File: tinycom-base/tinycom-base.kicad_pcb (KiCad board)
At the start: 2 copper layers, 45.2 x 45.2 mm, 48 parts, among them J1 MICRO_SD_HINGE, P1 CONN_02X10, P2 CONN_02X10, P3 USB_A, P4 USB_OTG, U1 SY8008BAAC, U2 AXP209, U3 SY8008BAAC, U4 RTL8188, U5 rainsun-antenna

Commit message: update base
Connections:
- P1 pad 1: (no net) -> HTX2P
- P1 pad 10: UD0_N -> UD1_N
- P1 pad 11: (no net) -> HTX0N
- P1 pad 12: UD1_P -> Net-(P1-Pad12)
- P1 pad 13: (no net) -> HTXCP
- P1 pad 14: UD1_N -> Net-(P1-Pad14)
- P1 pad 15: (no net) -> HTXCN
- P1 pad 16: (no net) -> Net-(P1-Pad16)
- P1 pad 17: (no net) -> HCEC
- P1 pad 18: (no net) -> HHPD
- P1 pad 19: (no net) -> HCSL
- P1 pad 20: (no net) -> HSDA
- P1 pad 3: (no net) -> HTX2N
- P1 pad 4: (no net) -> UD0_P
- P1 pad 5: (no net) -> HTX1P
- P1 pad 6: (no net) -> UD0_N
- P1 pad 7: (no net) -> HTX1N
- P1 pad 8: UD0_P -> UD1_P
- P1 pad 9: (no net) -> HTX0P
- P2 pad 13: (no net) -> Net-(P2-Pad13)
- P2 pad 15: (no net) -> UART1_RX
- P2 pad 17: (no net) -> UART1_TX
- P2 pad 8: (no net) -> Net-(P2-Pad8)
- P4 pad 2: (no net) -> Net-(P4-Pad2)
- P4 pad 3: (no net) -> Net-(P4-Pad3)
- U2 pad 11: (no net) -> Net-(U2-Pad11)
- U2 pad 19: (no net) -> Net-(U2-Pad19)
- U2 pad 20: (no net) -> Net-(U2-Pad20)
- U2 pad 25: (no net) -> Net-(U2-Pad25)
- U2 pad 29: (no net) -> Net-(U2-Pad29)
- U2 pad 3: (no net) -> Net-(U2-Pad3)
- U2 pad 36: (no net) -> Net-(U2-Pad36)
- U2 pad 38: (no net) -> Net-(U2-Pad38)
- U2 pad 39: (no net) -> Net-(U2-Pad39)
- U2 pad 41: (no net) -> Net-(U2-Pad41)
- U2 pad 42: (no net) -> Net-(U2-Pad42)
- U2 pad 43: (no net) -> Net-(U2-Pad43)
- U2 pad 45: (no net) -> Net-(U2-Pad45)
- U2 pad 5: (no net) -> Net-(U2-Pad5)
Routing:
- net UD0_N: track 39.4 -> 41.4 mm
- net UD0_P: track 40.9 -> 42.9 mm
- net UD1_P: track 18.0 -> 16.2 mm
- net UD1_N: track 18.5 -> 16.7 mm

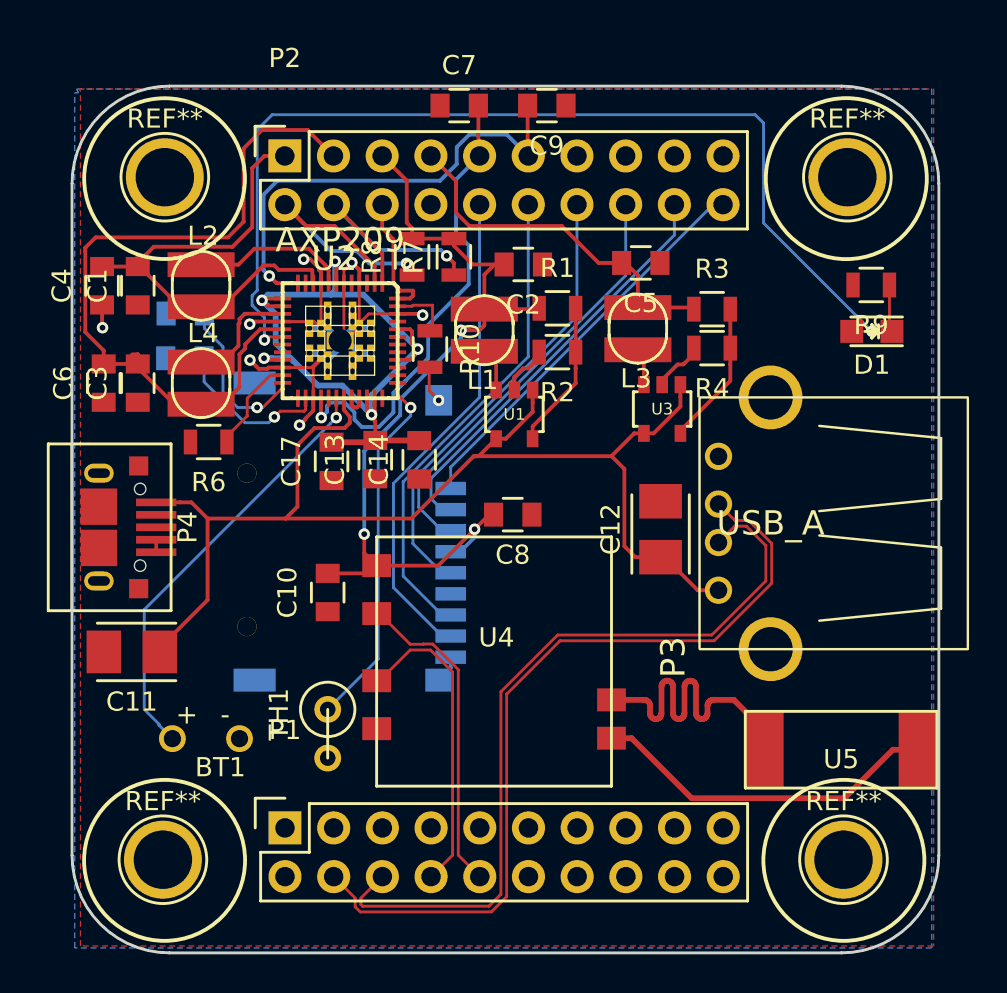
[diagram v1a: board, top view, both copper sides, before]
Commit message: update base power
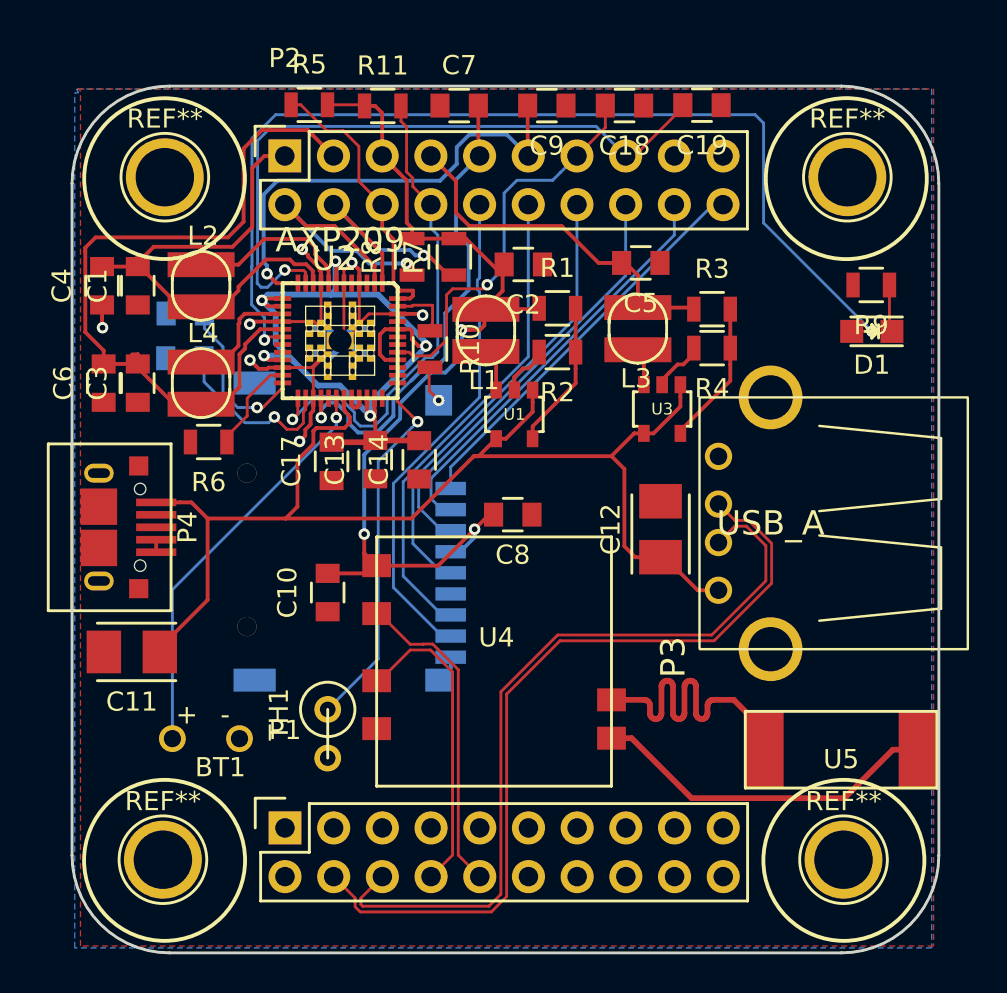
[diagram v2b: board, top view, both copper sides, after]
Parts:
- added C18: 10uF, Capacitors_SMD:C_0805, F.Cu at (153.3, 80.3)
- added C19: 0uF, Capacitors_SMD:C_0805, F.Cu at (157.3, 80.2)
- added R11: 10K, Resistors_SMD:R_0805, F.Cu at (140.7, 80.3)
- added R5: 47K, Resistors_SMD:R_0805, F.Cu at (136.8, 80.2)
- U2: footprint tinycom:ax209 -> tinycom:axp209
- moved L1 0.08 mm to (146.0, 92.0)
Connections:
- net UART1_TX renamed Net-(P2-Pad17)
- P2 pad 13: Net-(P2-Pad13) -> LDO3_28
- P2 pad 15: UART1_RX -> LDO4_28
- P2 pad 8: Net-(P2-Pad8) -> RESET_N
- U2 pad 11: Net-(U2-Pad11) -> LDO4_28
- U2 pad 25: Net-(U2-Pad25) -> RESET_N
- U2 pad 41: Net-(U2-Pad41) -> LDO3_28
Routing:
- net LDO4_28: track 0.00 -> 35.3 mm, vias 0 -> 1
- net RESET_N: track 0.00 -> 25.9 mm, vias 0 -> 1
- net LDO3_28: track 0.00 -> 20.7 mm, vias 0 -> 1
- net NMI_N: track 6.66 -> 14.6 mm
- net VCC_33: track 44.2 -> 50.0 mm
- net IPSOUT: track 42.6 -> 46.0 mm
- net Net-(BT1-Pad1): track 22.5 -> 21.3 mm
- net GND: track 52.4 -> 53.6 mm
- net Net-(C15-Pad2): track 8.29 -> 9.16 mm
- net Net-(L2-Pad1): track 8.20 -> 8.86 mm
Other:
- net class Power: clearance 0.15 -> 0.14; trace_width 0.2 -> 0.15

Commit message: update a20+base (connect reset)
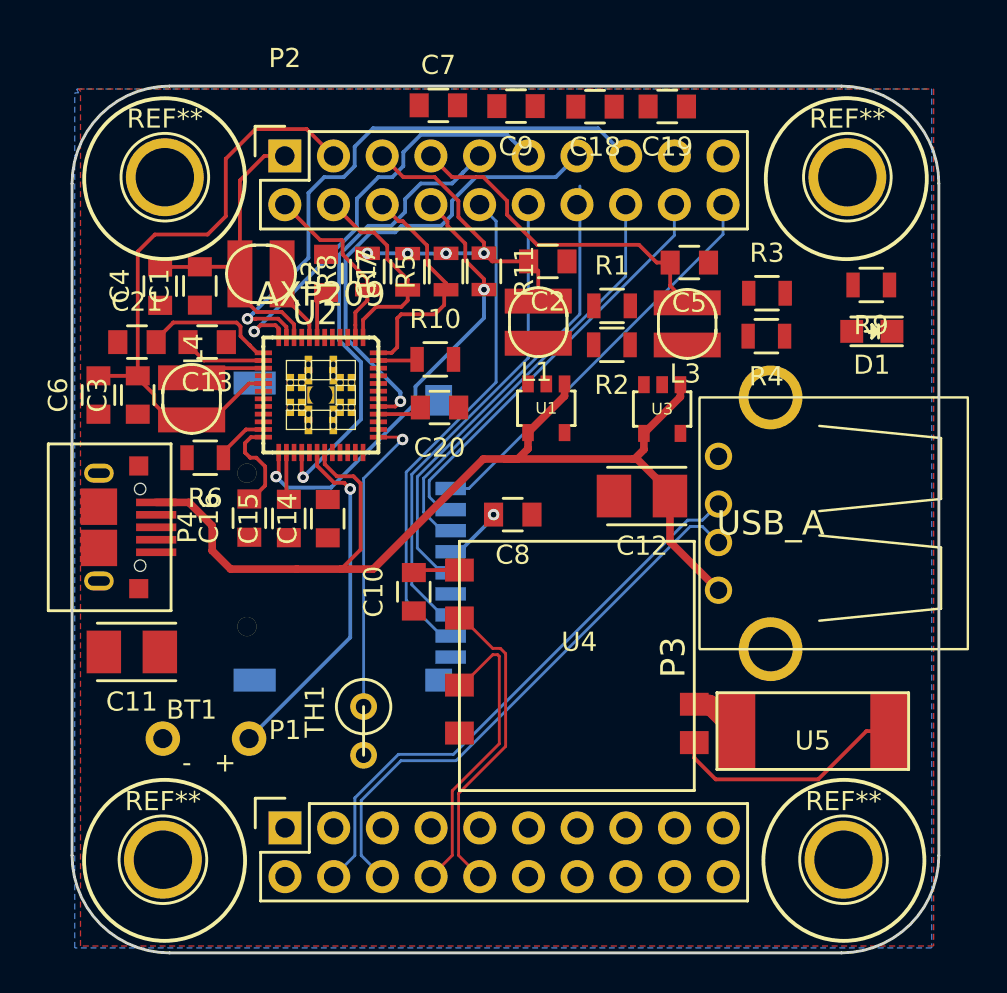
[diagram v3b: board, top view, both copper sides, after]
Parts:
- added C20: 10uF, Capacitors_SMD:C_0805, F.Cu at (143.6, 96.0)
- added C21: 10uF, Capacitors_SMD:C_0805, F.Cu at (127.8, 92.6)
- C15, C16: moved to F.Cu
- moved R5 11.2 mm to (144.0, 88.9), turned to 90 degrees
- moved C16 11.2 mm to (133.7, 101.8), turned to 90 degrees
- moved C13 10.7 mm to (131.5, 92.6), turned to 180 degrees
- moved R11 10.1 mm to (145.9, 88.9), turned to 270 degrees
- moved C15 9.96 mm to (135.8, 101.8), turned to 90 degrees
- moved C17 9.80 mm to (137.7, 89.0), turned to 270 degrees
- moved C14 5.67 mm to (137.8, 101.8)
- moved C10 4.49 mm to (142.3, 105.6)
- moved U4 4.33 mm to (150.7, 109.2)
- moved C1 3.24 mm to (131.1, 89.7)
- moved L2 3.19 mm to (134.3, 89.0), turned to 270 degrees
- moved C4 3.03 mm to (129.1, 89.7)
- moved U2 3.00 mm to (137.4, 95.4)
- moved R3 2.98 mm to (160.7, 90.1)
- moved R4 2.90 mm to (160.7, 92.3)
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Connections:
- C13 pad 1: GND -> Net-(C13-Pad1)
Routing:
- net Net-(D1-Pad2): track 53.7 -> 0.00 mm, vias 2 -> 0
- net GND: track 53.6 -> 0.00 mm, vias 8 -> 0
- net IPSOUT: track 46.0 -> 16.6 mm, vias 5 -> 0
- net VCC_33: track 50.0 -> 25.1 mm, vias 3 -> 5
- net Net-(U4-Pad6): track 18.1 -> 2.76 mm
- net UD0_P: track 42.9 -> 29.9 mm
- net UD0_N: track 41.4 -> 29.3 mm
- net VCC_12_CPU: track 26.2 -> 17.3 mm
- net Net-(R1-Pad2): track 7.73 -> 0.00 mm
- net Net-(R3-Pad2): track 7.56 -> 0.00 mm
- net +5V: track 63.9 -> 56.6 mm
- net Net-(C15-Pad2): track 9.16 -> 2.49 mm, vias 1 -> 0
- net VCC_12_INT: track 38.8 -> 32.4 mm
- net Net-(U4-Pad5): track 18.3 -> 12.5 mm
- net TWI0_SCK: track 15.4 -> 9.63 mm, vias 1 -> 0
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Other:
- net class Default: trace_width 0.15 -> 0.2
- net class Power: trace_width 0.15 -> 0.2

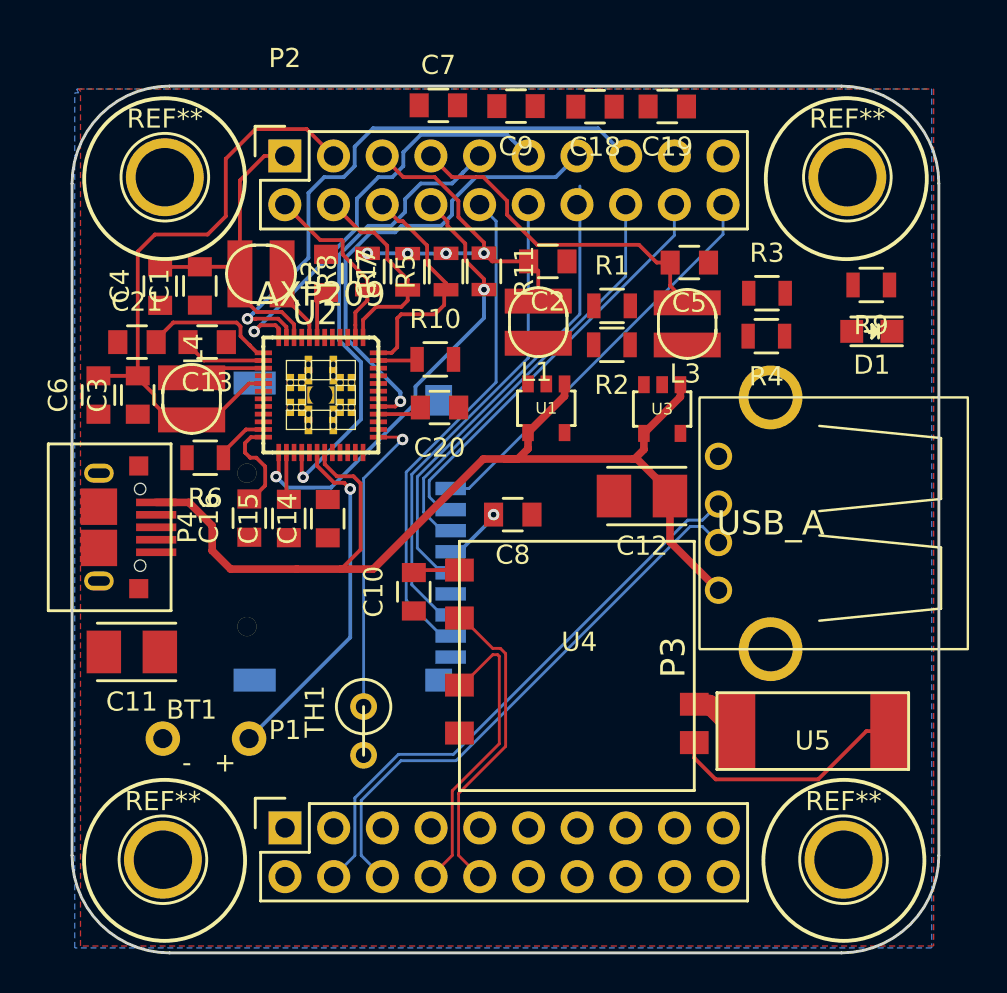
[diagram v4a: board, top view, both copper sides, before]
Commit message: a20 remove bottom components
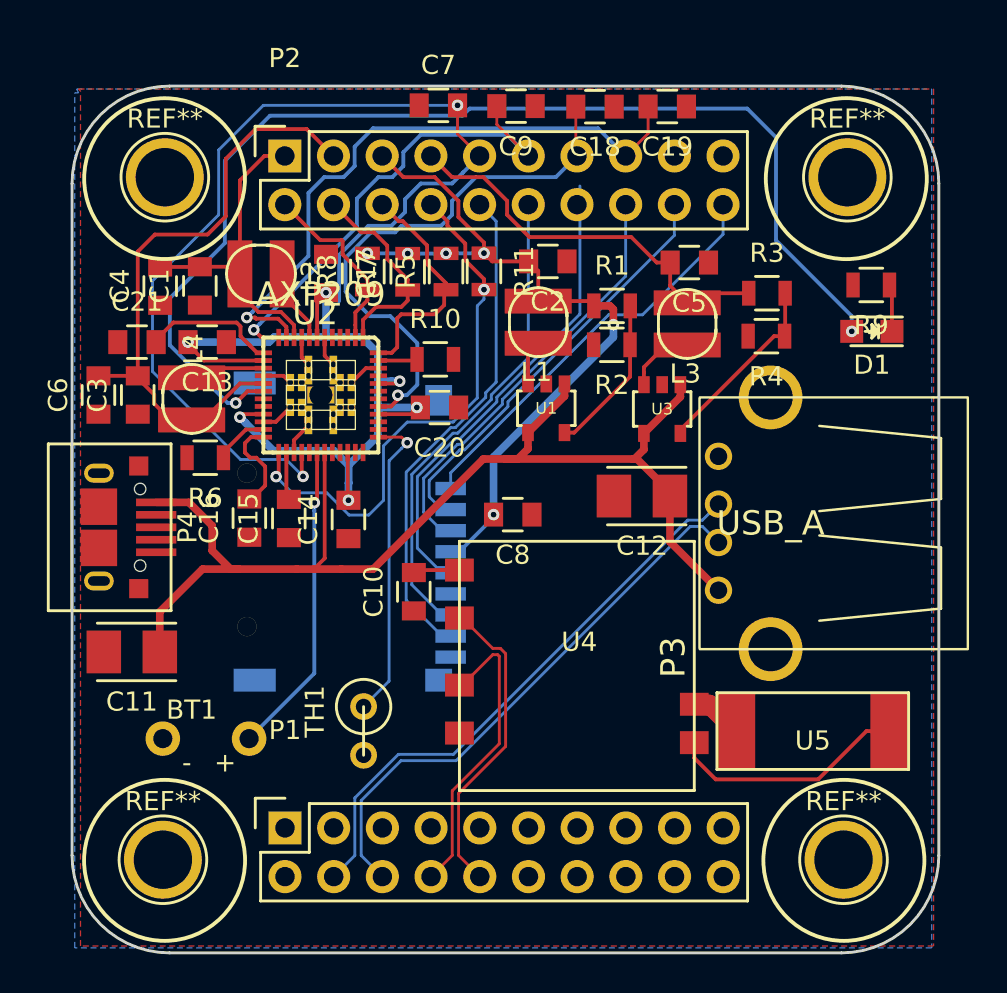
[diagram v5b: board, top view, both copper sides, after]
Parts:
- moved C14 1.08 mm to (138.9, 101.9)
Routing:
- net Net-(D1-Pad2): track 0.00 -> 59.4 mm, vias 0 -> 2
- net IPSOUT: track 16.6 -> 52.8 mm, vias 0 -> 6
- net VCC_13_RTC: track 24.5 -> 53.2 mm, vias 1 -> 2
- net VCC_33: track 25.1 -> 42.5 mm, vias 5 -> 6
- net Net-(R3-Pad2): track 0.00 -> 9.90 mm
- net GND: track 0.00 -> 9.82 mm
- net Net-(R1-Pad2): track 0.00 -> 8.33 mm
- net +5V: track 56.6 -> 62.2 mm
- net RESET_N: track 23.6 -> 28.2 mm
- net LDO3_28: track 24.6 -> 28.9 mm
- net Net-(L3-Pad1): track 0.00 -> 3.65 mm
- net VCC_15: track 17.7 -> 21.1 mm
- net LDO4_28: track 29.8 -> 32.8 mm
- net VCC_30_ANL: track 22.3 -> 25.0 mm
- net Net-(D1-Pad1): track 0.00 -> 2.47 mm
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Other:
- net class Default: trace_width 0.2 -> 0.4
- net class Power: trace_width 0.2 -> 0.4

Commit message: base drc
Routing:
- net GND: track 9.82 -> 48.3 mm, vias 0 -> 29
- net VCC_33: track 42.5 -> 46.6 mm
- net IPSOUT: track 52.8 -> 55.5 mm
- net Net-(U2-Pad32): track 0.00 -> 1.98 mm
- net VCC_12_INT: track 32.4 -> 33.0 mm
- net SDC0_D2: track 21.7 -> 21.1 mm
- net SDC0_CLK: track 24.8 -> 24.2 mm
- net LDO3_28: track 28.9 -> 28.3 mm
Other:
- net class Default: trace_width 0.4 -> 0.15

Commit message: improve base
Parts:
- added C22: 0.22uF, Capacitors_SMD:C_0805, F.Cu at (140.9, 102.4)
- added C23: 4.7uF, Capacitors_SMD:C_0805, F.Cu at (135.5, 102.5)
- added C24: 0.22uF, Capacitors_SMD:C_0805, F.Cu at (131.3, 97.8)
- added C25: 100pF, Capacitors_SMD:C_0805, F.Cu at (143.4, 92.0)
- added C26: 22uF, Capacitors_SMD:C_0805, F.Cu at (146.6, 96.1)
- added C27: 22uF, Capacitors_SMD:C_0805, F.Cu at (152.7, 96.2)
- added C28: 22pF, Capacitors_SMD:C_0805, F.Cu at (152.5, 88.4)
- added C29: 22pF, Capacitors_SMD:C_0805, F.Cu at (160.7, 88.2)
- added R12: 2.2R, Resistors_SMD:R_0805, F.Cu at (137.2, 102.5)
- added R13: 1R, Resistors_SMD:R_0805, F.Cu at (128.1, 92.2)
- C1, C3: value C_Small -> 10uF
- C17: value 10uF -> 2.2uF
- C2, C5: value C_Small -> 22uF
- C4, C6: value C_Small -> 1nF
- moved C21 3.59 mm to (126.4, 89.3), turned to 270 degrees
- moved C15 2.25 mm to (133.7, 102.6)
- moved C16 2.08 mm to (131.7, 102.4), turned to 270 degrees
- moved C10 1.19 mm to (142.3, 106.8)
- moved R6 1.12 mm to (131.3, 99.8)
- moved C14 0.65 mm to (139.3, 102.4)
- moved C2 0.57 mm to (148.7, 88.3)
- moved L4 0.49 mm to (130.7, 95.1)
- moved C13 0.40 mm to (131.5, 92.2), turned to 0 degrees
- moved C4 0.29 mm to (129.0, 89.4)
- moved C1 0.27 mm to (131.0, 89.4)
- moved C6 0.27 mm to (125.8, 95.1)
- moved C3 0.26 mm to (127.8, 95.1)
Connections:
- C13 pad 1: Net-(C13-Pad1) -> GND
- C16 pad 1: GND -> Net-(C16-Pad1)
- C16 pad 2: Net-(C16-Pad2) -> GND
- C21 pad 2: IPSOUT -> Net-(C21-Pad2)
- U1 pad 1: +5V -> IPSOUT
- U1 pad 4: +5V -> IPSOUT
- U2 pad 13: IPSOUT -> Net-(C21-Pad2)
- U2 pad 24: Net-(C16-Pad2) -> Net-(C16-Pad1)
- U3 pad 1: +5V -> IPSOUT
- U3 pad 4: +5V -> IPSOUT
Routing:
- net IPSOUT: track 55.5 -> 80.7 mm, vias 6 -> 7
- net GND: track 48.3 -> 63.9 mm, vias 29 -> 39
- net Net-(C21-Pad2): track 0.00 -> 11.3 mm
- net VCC_13_RTC: track 53.3 -> 42.1 mm
- net +5V: track 62.2 -> 51.7 mm
- net Net-(C16-Pad1): track 0.00 -> 7.12 mm
- net Net-(C16-Pad2): track 5.04 -> 0.00 mm
- net VCC_12_INT: track 33.0 -> 36.6 mm
- net VCC_33: track 46.6 -> 50.0 mm
- net VCC_15: track 21.1 -> 24.1 mm
- net Net-(C28-Pad1): track 8.33 -> 10.4 mm
- net Net-(C23-Pad2): track 0.00 -> 1.84 mm
- net Net-(C29-Pad1): track 9.90 -> 11.7 mm
- net Net-(D1-Pad2): track 59.4 -> 61.0 mm
- net Net-(C25-Pad1): track 2.04 -> 3.58 mm
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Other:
- net class Default: trace_width 0.15 -> 0.2

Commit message: update pic base
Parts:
- added D2: D_Schottky_Small, tinycom:SMA-KA, F.Cu at (134.0, 106.8)
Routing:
- net GND: vias 39 -> 40
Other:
- net class Default: trace_width 0.2 -> 0.4
